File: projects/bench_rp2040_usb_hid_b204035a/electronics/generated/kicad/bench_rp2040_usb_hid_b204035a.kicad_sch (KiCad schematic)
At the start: 10 parts, among them J1 USB-C POWER, J2 SWD 10-pin, U1 3V3 LDO, U2 RP2040, U3 2MB QSPI, X1 12MHz XTAL

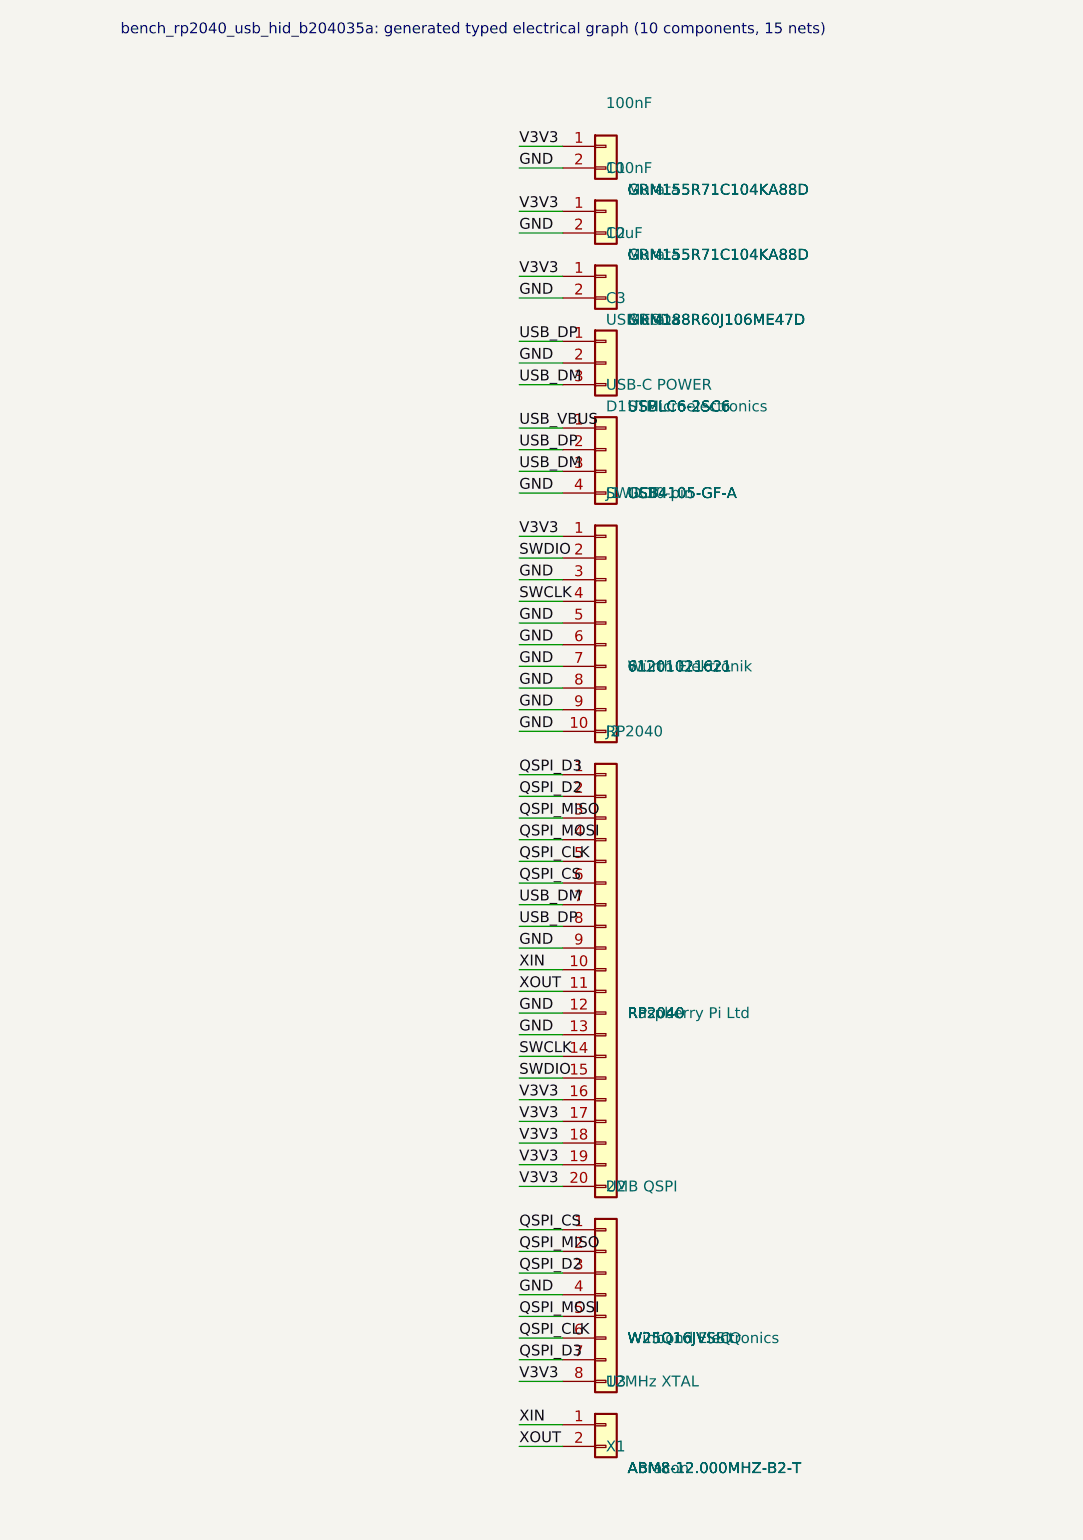
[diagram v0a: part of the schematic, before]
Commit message: fix: model rp2040 usb esd boundary
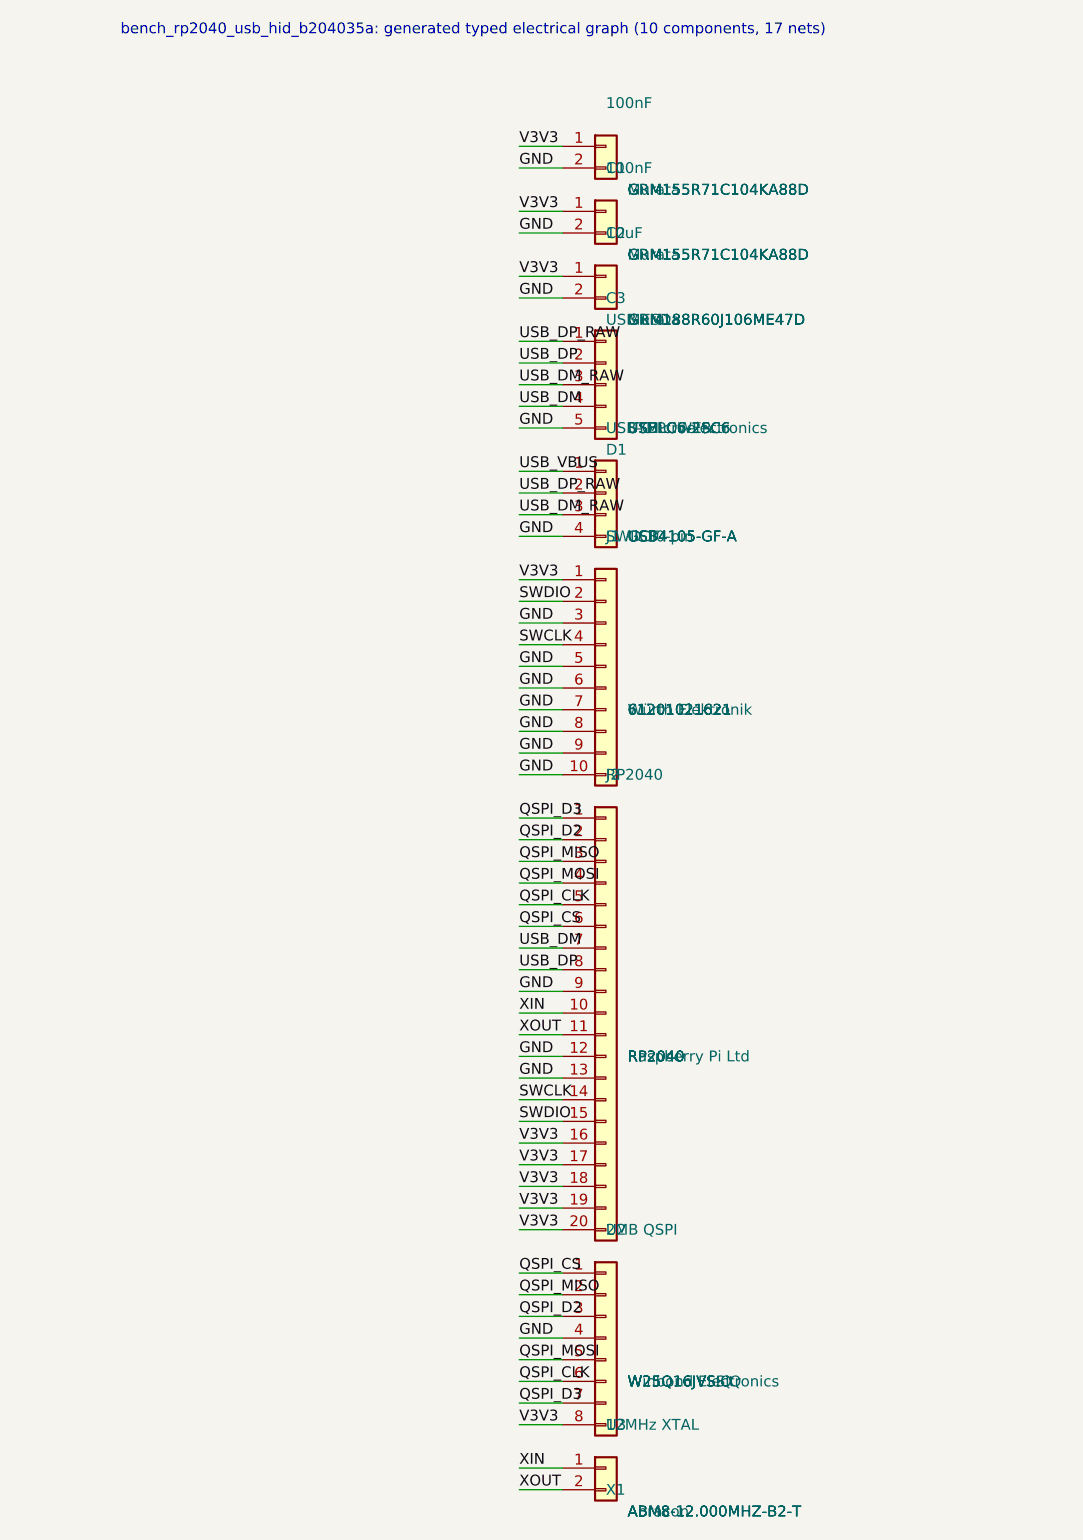
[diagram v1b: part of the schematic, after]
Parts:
- D1: symbol Connector_Generic:Conn_01x03 -> Connector_Generic:Conn_01x05
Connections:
- net GND: now also D1.5 (Pin_5); no longer D1.2 (Pin_2)
- net USB_DM: now also D1.4 (Pin_4); no longer D1.3 (Pin_3), J1.3 (Pin_3)
- net USB_DP: now also D1.2 (Pin_2); no longer D1.1 (Pin_1), J1.2 (Pin_2)
- new net USB_DM_RAW: D1.3 (Pin_3), J1.3 (Pin_3)
- new net USB_DP_RAW: D1.1 (Pin_1), J1.2 (Pin_2)
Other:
- note added: "bench_rp2040_usb_hid_b204035a: generated typed electrical graph (10 components, 17 nets)"
- note removed: "bench_rp2040_usb_hid_b204035a: generated typed electrical graph (10 components, 15 nets)"

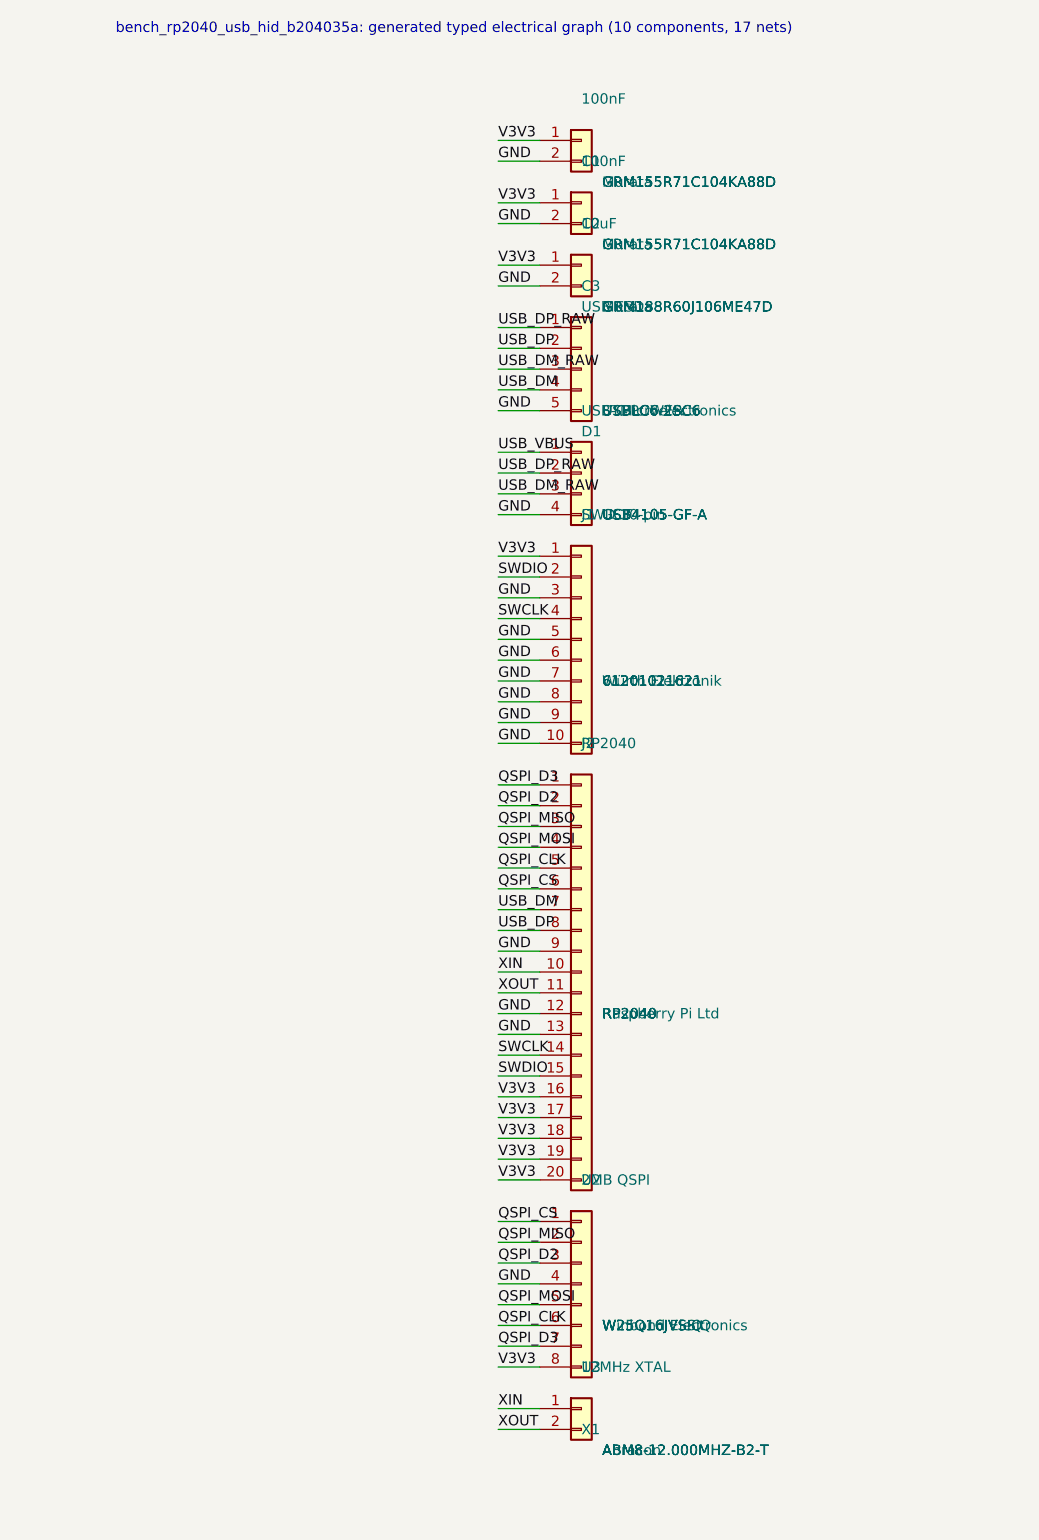
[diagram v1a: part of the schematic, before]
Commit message: fix: ground rp2040 power path evidence
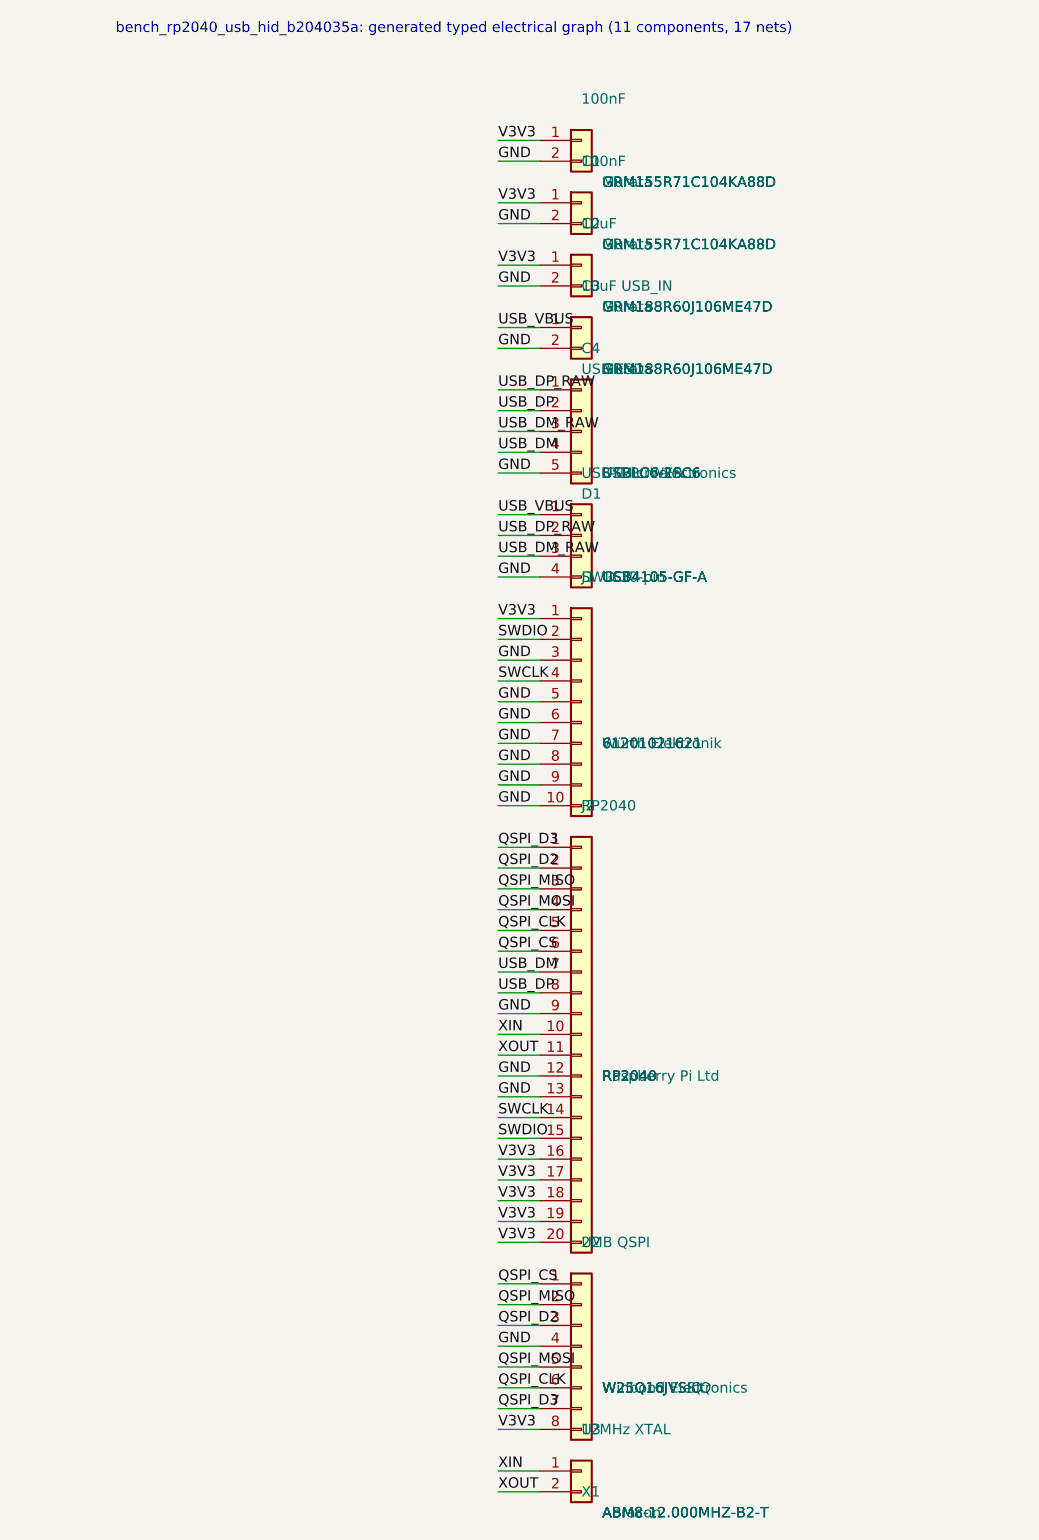
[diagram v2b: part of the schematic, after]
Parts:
- added D1: USB ESD, Package_TO_SOT_SMD:SOT-23-6, symbol Connector_Generic:Conn_01x05
- C4: renamed from D1; value USB ESD -> 10uF USB_IN; footprint Package_TO_SOT_SMD:SOT-23-6 -> Capacitor_SMD:C_0603_1608Metric; symbol Connector_Generic:Conn_01x05 -> Connector_Generic:Conn_01x02; MPN USBLC6-2SC6 -> GRM188R60J106ME47D; Manufacturer STMicroelectronics -> Murata; Supplier_SKU USBLC6-2SC6 -> GRM188R60J106ME47D
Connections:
- net GND: now also C4.2 (Pin_2), D1.5 (Pin_5); no longer C4.5 (Pin_5)
- net USB_DM: now also D1.4 (Pin_4); no longer C4.4 (Pin_4)
- net USB_DM_RAW: now also D1.3 (Pin_3); no longer C4.3 (Pin_3)
- net USB_DP: now also D1.2 (Pin_2); no longer C4.2 (Pin_2)
- net USB_DP_RAW: now also D1.1 (Pin_1); no longer C4.1 (Pin_1)
- net USB_VBUS: now also C4.1 (Pin_1)
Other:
- note added: "bench_rp2040_usb_hid_b204035a: generated typed electrical graph (11 components, 17 nets)"
- note removed: "bench_rp2040_usb_hid_b204035a: generated typed electrical graph (10 components, 17 nets)"
